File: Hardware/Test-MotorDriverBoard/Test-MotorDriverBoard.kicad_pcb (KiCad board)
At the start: 2 copper layers, 10 x 9.5 mm, 12 parts, among them T1 NDS332P, T10 TEST_PAD, T2 PMF370XN,115, T3 NDS332P, T4 PMF370XN,115, T5 TEST_PAD, T6 TEST_PAD, T7 TEST_PAD, T8 TEST_PAD, T9 TEST_PAD

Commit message: Minor Components changes
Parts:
- renumbered T5 to Ts5, T6 to Ts6, T7 to Ts7, T8 to Ts8
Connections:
- T10 pad 1: /Motor_B -> Net-(T10-Pad1)
- T9 pad 1: /Motor_A -> Net-(T9-Pad1)
- Ts6 pad 1: GND -> /Input_1
- Ts7 pad 1: /Input_1 -> /Input_2
- Ts8 pad 1: /Input_2 -> GND
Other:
- board size 10 x 9.5 mm -> 9.9 x 10 mm

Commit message: minor changes to the motor test board
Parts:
- renumbered T10 to Ts10, T9 to Ts9
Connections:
- Ts10 pad 1: Net-(T10-Pad1) -> /Motor_B
- Ts6 pad 1: /Input_1 -> GND
- Ts7 pad 1: /Input_2 -> /Input_1
- Ts8 pad 1: GND -> /Input_2
- Ts9 pad 1: Net-(T9-Pad1) -> /Motor_A
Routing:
- net +3V3: track 14.3 -> 15.4 mm
- net GND: track 12.8 -> 13.8 mm, vias 1 -> 2
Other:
- board text added: "H-Bridge Test REV 0"
- board text added: "HDE ■■■"

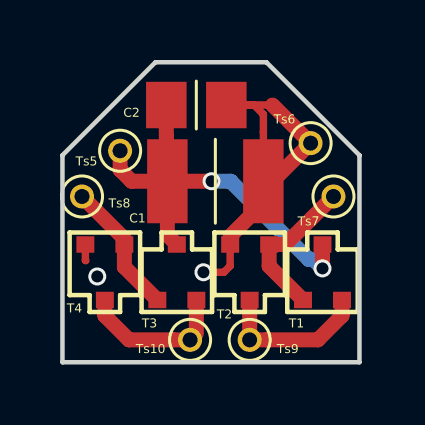
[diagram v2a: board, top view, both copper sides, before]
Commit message: added the current changes from the test motor
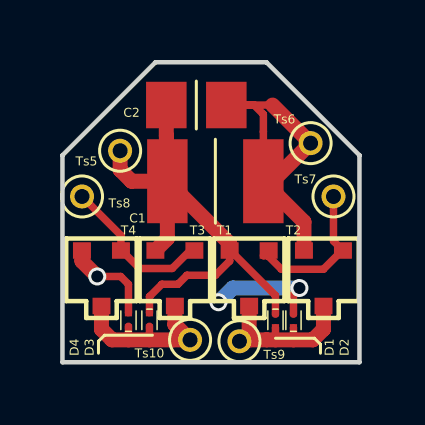
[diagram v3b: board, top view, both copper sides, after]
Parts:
- added D1: PMEG1201AESF, HDEP_Diodes:SOD962-2, F.Cu at (143.1, 113.6)
- added D2: PMEG1201AESF, HDEP_Diodes:SOD962-2, F.Cu at (143.7, 113.6)
- added D3: PMEG1201AESF, HDEP_Diodes:SOD962-2, F.Cu at (138.9, 113.6)
- added D4: PMEG1201AESF, HDEP_Diodes:SOD962-2, F.Cu at (138.2, 113.6)
- moved T2 2.47 mm to (144.7, 112.2)
- moved T1 2.45 mm to (142.2, 112.2), turned to 90 degrees
- moved Ts9 0.34 mm to (141.9, 114.3)
- moved T4 0.23 mm to (137.3, 112.2)
- moved T3 0.21 mm to (139.7, 112.2), turned to 90 degrees
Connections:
- T1 pad 2: /Motor_A -> +3V3
- T1 pad 3: +3V3 -> /Motor_A
- T3 pad 2: /Motor_B -> +3V3
- T3 pad 3: +3V3 -> /Motor_B
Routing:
- net GND: track 13.8 -> 18.6 mm, vias 2 -> 3
- net +3V3: track 15.4 -> 19.1 mm, vias 2 -> 0
- net /Motor_A: track 5.27 -> 7.56 mm
- net /Motor_B: track 5.11 -> 6.12 mm
- net /Input_2: track 4.49 -> 5.28 mm
